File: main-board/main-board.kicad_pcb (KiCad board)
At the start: 2 copper layers, 180 x 111 mm, 63 parts, among them J1 INPUT, J2 NC1, J3 OUTPUT, J4 Conn_01x03_Pin, J5 COM, J6 INPUT_DEBUG, J7 NC__DEBUG, J8 OUTPUT_DEBUG, SW1 SW_SPST, SW2 Power Switch A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

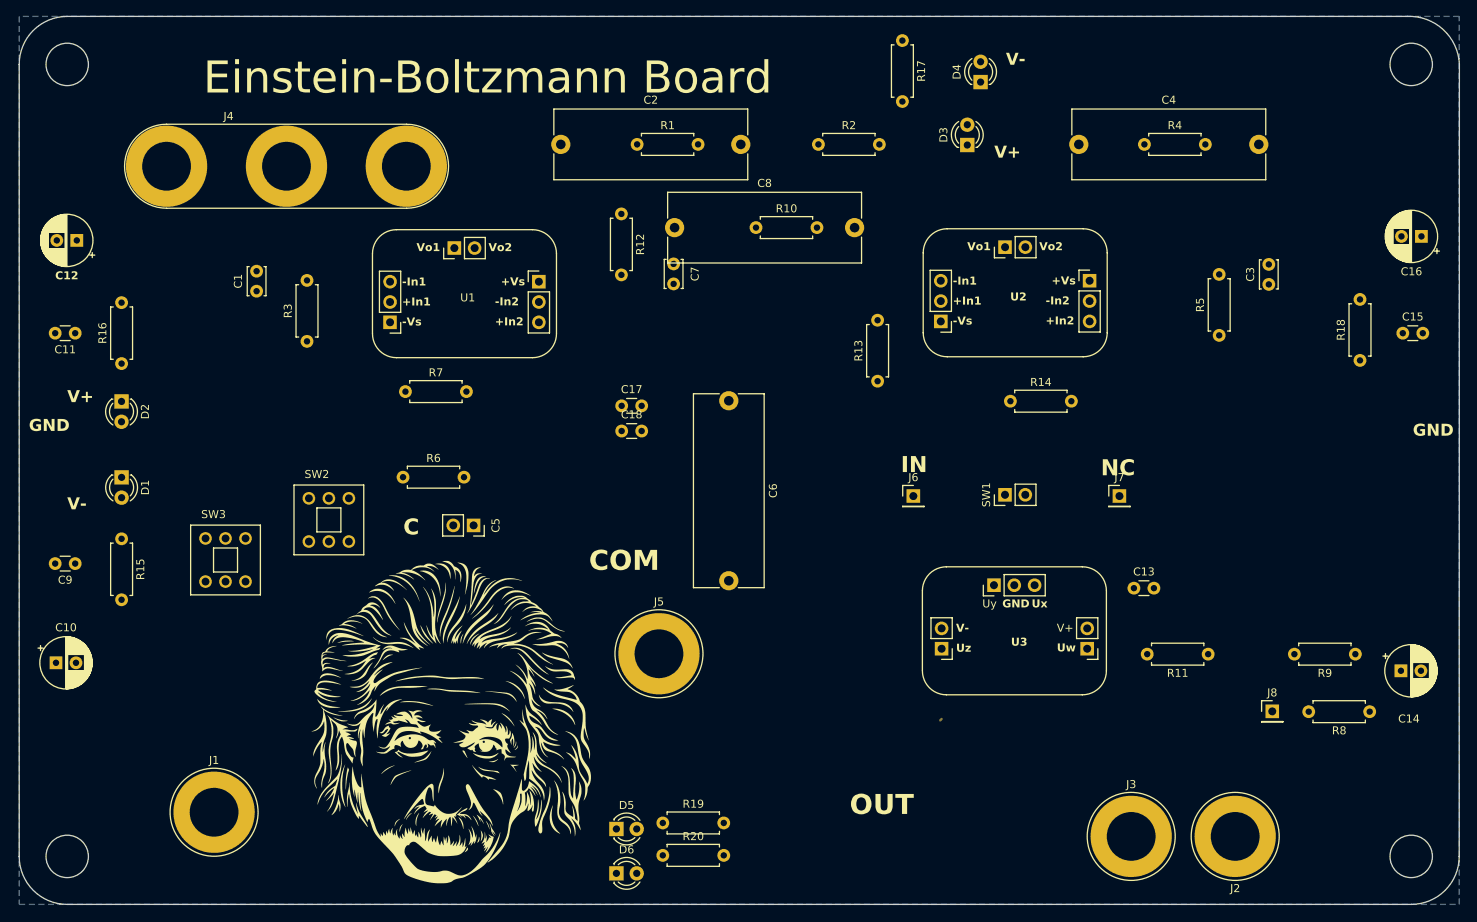
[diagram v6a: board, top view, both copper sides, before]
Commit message: Improves components displacement
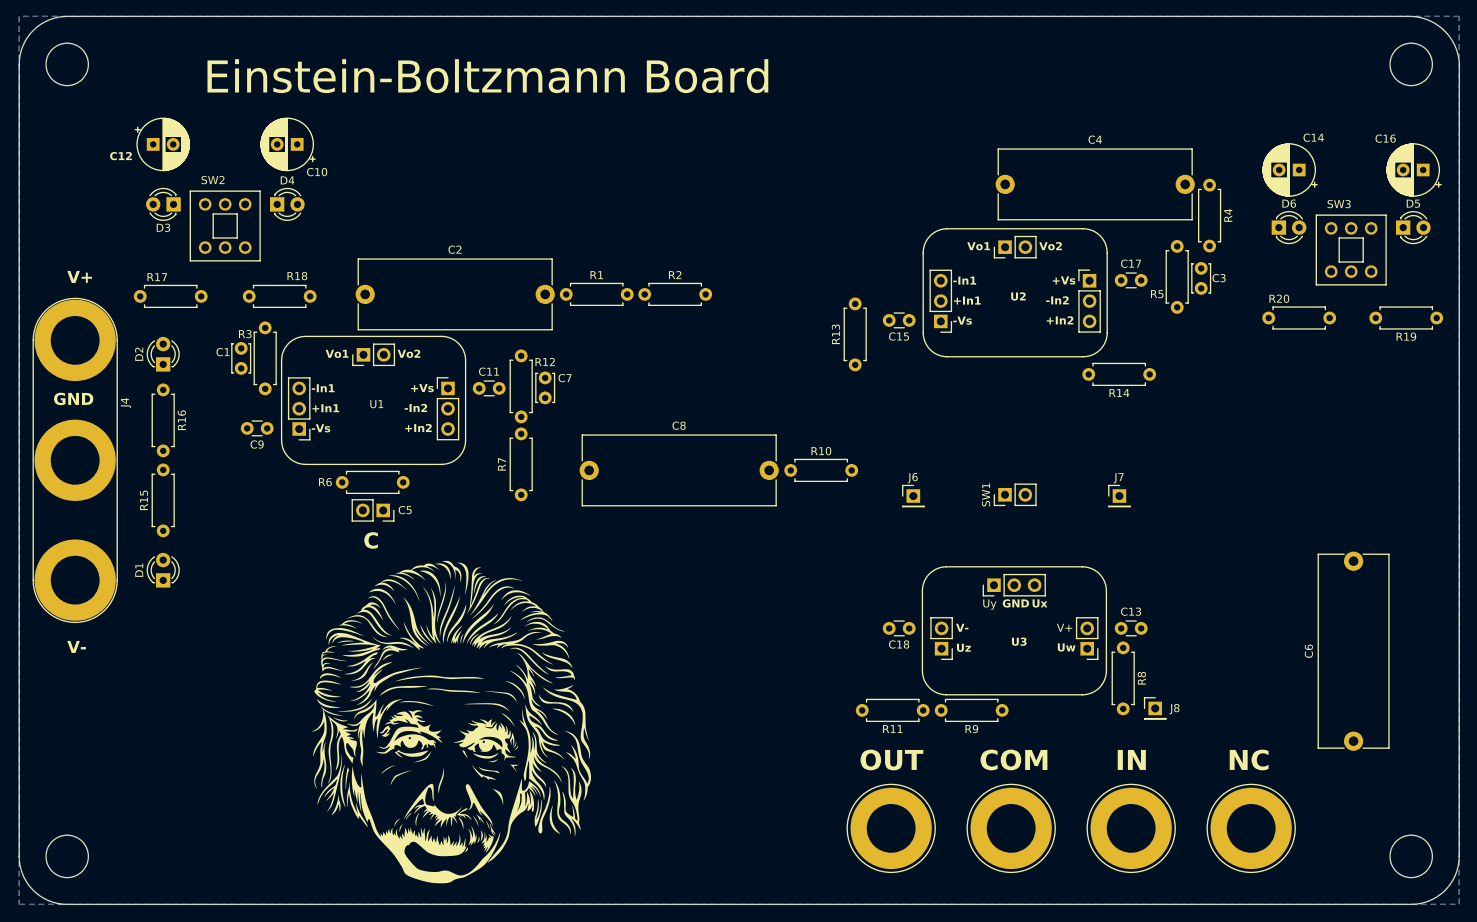
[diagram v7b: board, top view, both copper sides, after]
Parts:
- moved SW3 145.9 mm to (224.0, 69.5)
- moved R18 131.5 mm to (96.4, 78.0), turned to 180 degrees
- moved D5 123.8 mm to (233.0, 69.4)
- moved D6 115.6 mm to (217.5, 69.4)
- moved R19 115.5 mm to (237.2, 80.7), turned to 180 degrees
- moved J1 114.7 mm to (199.0, 144.5)
- moved R20 101.2 mm to (216.2, 80.7)
- moved R17 100.5 mm to (75.1, 78.0), turned to 0 degrees
- moved D3 99.5 mm to (79.3, 66.5), turned to 180 degrees
- moved D4 89.2 mm to (92.2, 66.5), turned to 0 degrees
- moved C6 88.9 mm to (226.8, 133.6), turned to 90 degrees
- moved C10 71.5 mm to (94.8, 59.0), turned to 180 degrees
- moved C17 64.4 mm to (197.8, 76.0)
- moved C14 63.9 mm to (220.0, 62.2), turned to 180 degrees
- moved C15 61.7 mm to (171.2, 81.0), turned to 180 degrees
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
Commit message: Continues placement process
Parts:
- removed C14, C16: 10u, Capacitor_THT:CP_Radial_D6.3mm_P2.50mm
- moved D3 75.8 mm to (74.1, 142.1), turned to 0 degrees
- moved D4 75.6 mm to (89.6, 142.1)
- moved SW2 75.6 mm to (80.6, 142.1)
- moved C10 75.0 mm to (70.0, 129.8), turned to 90 degrees
- moved R18 60.4 mm to (92.1, 138.3)
- moved R17 60.3 mm to (74.1, 138.3)
- moved J1 43.2 mm to (155.8, 146.0)
- moved R19 37.0 mm to (206.6, 59.9)
- moved R20 34.7 mm to (188.4, 59.9)
- moved J3 31.8 mm to (200.8, 146.0)
- moved D5 29.5 mm to (204.1, 63.6)
- moved D6 29.5 mm to (188.5, 63.6)
- moved SW3 29.5 mm to (195.1, 63.8)
- moved J2 28.2 mm to (185.8, 146.0)
- moved R2 26.1 mm to (163.3, 85.0), turned to 90 degrees
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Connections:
- C10 pad 2: -9VA -> -9V
- C12 pad 1: +9VA -> +9V
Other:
- board size 180 x 111 mm -> 161.8 x 100 mm
- board text added: "+9V"
- board text added: "+9VA"
- board text added: "+9VB"
- board text added: "-9V"
- board text added: "-9VA"
- board text added: "-9VB"
- board text added: "U1 - PWR"
- board text added: "U2 and U3 - PWR"
- board text removed: "V+"
- board text removed: "V-"
